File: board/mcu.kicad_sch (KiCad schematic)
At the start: 1 part, among them U101 STM32G0B0CETx

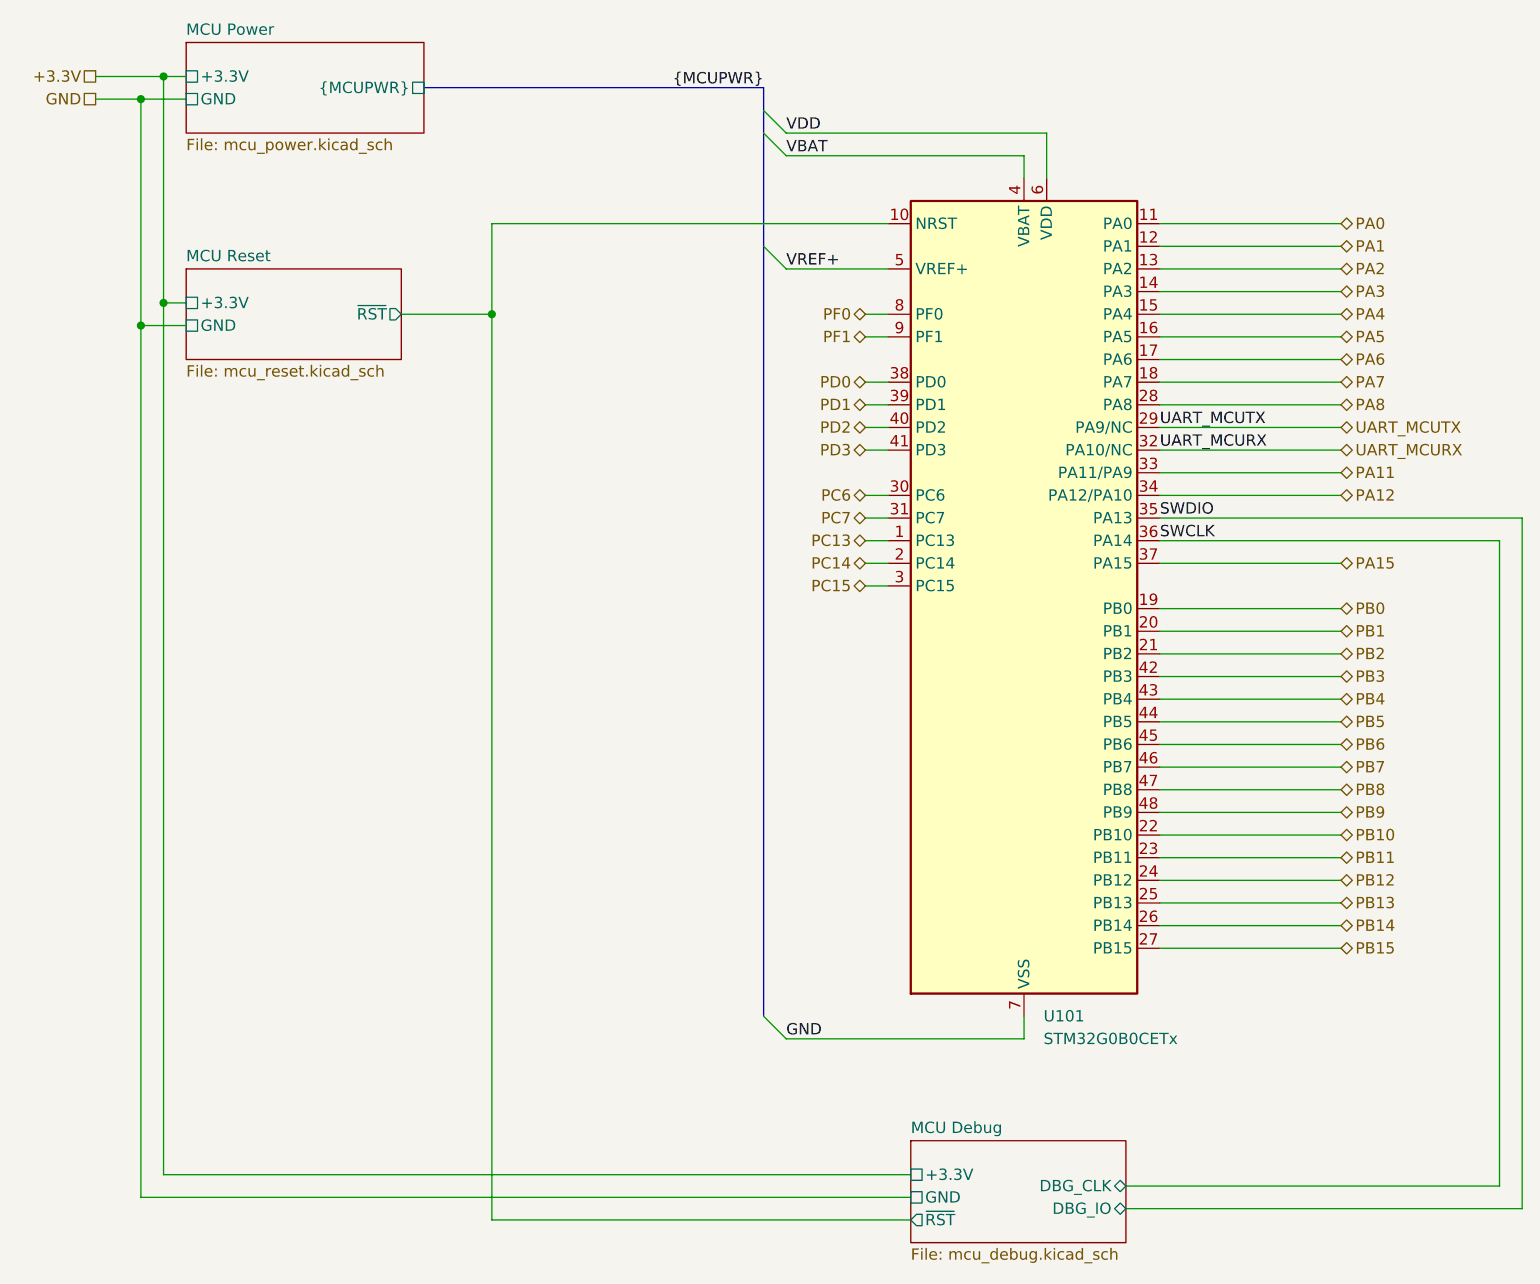
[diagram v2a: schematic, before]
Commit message: redo board to use I2C port expanders (and smaller MCU)
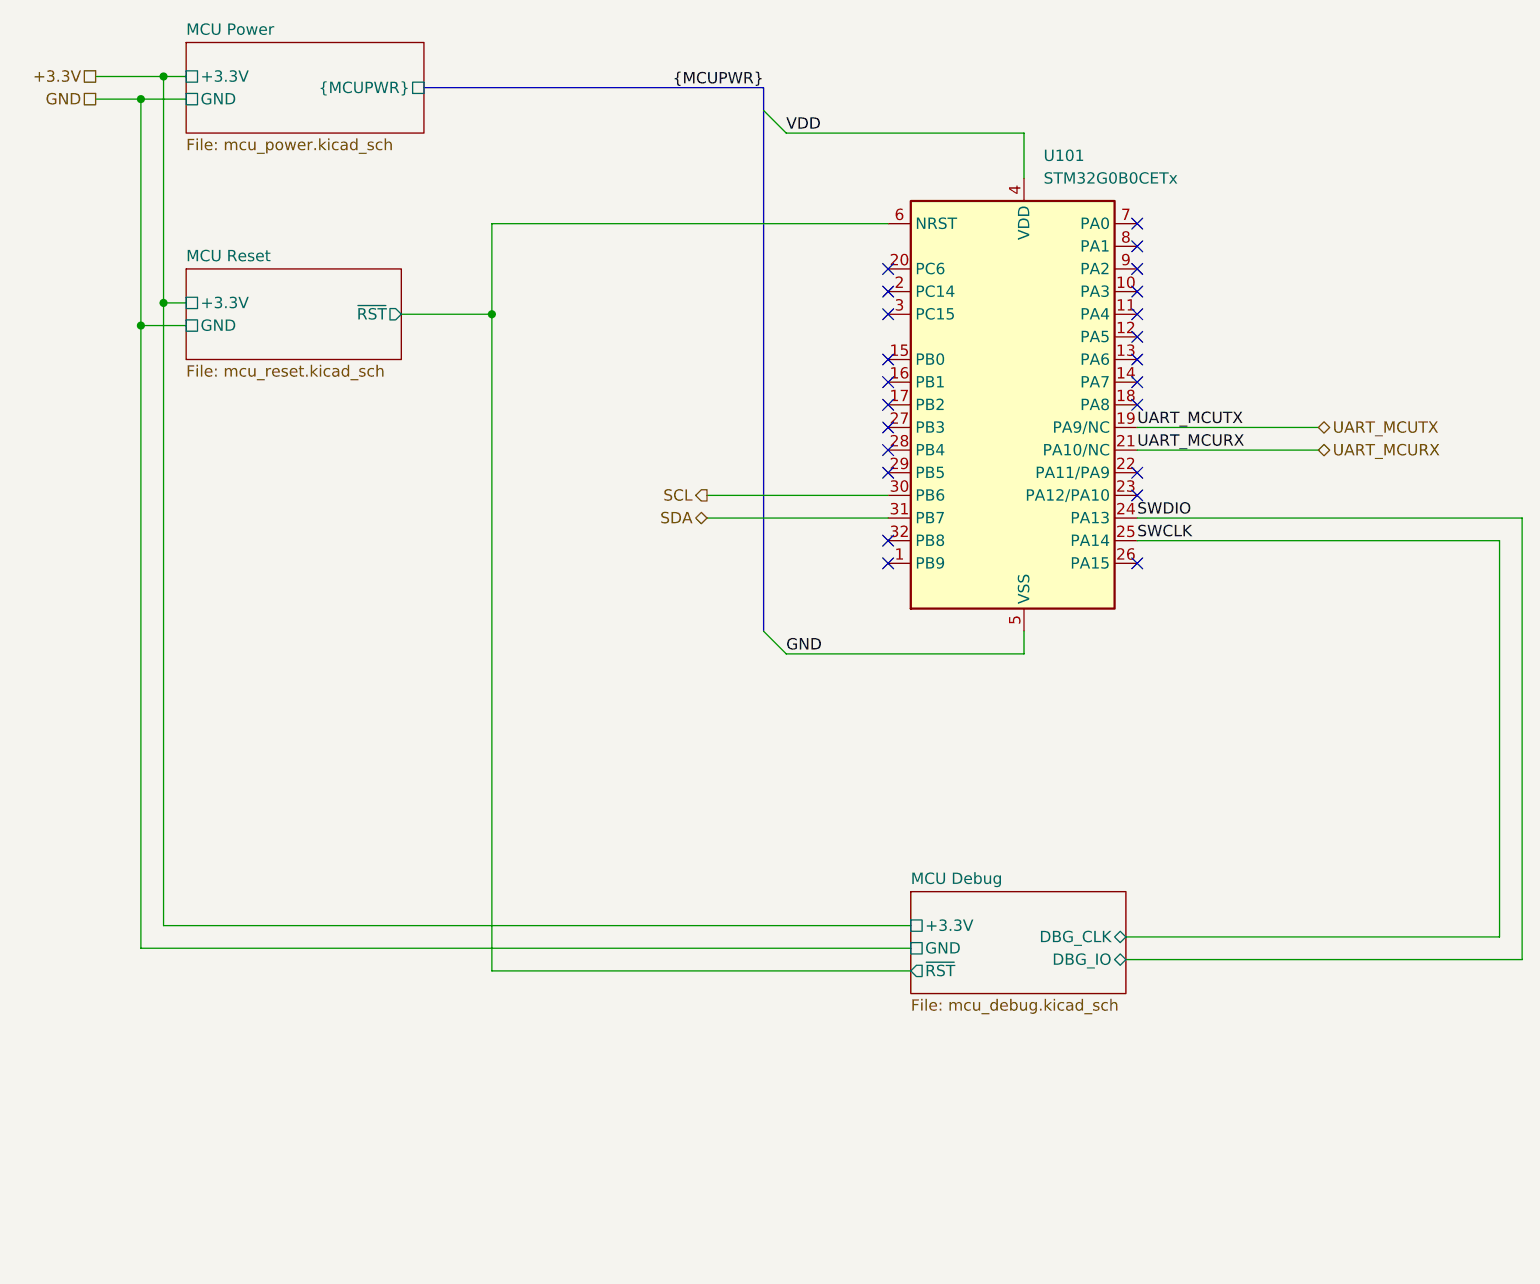
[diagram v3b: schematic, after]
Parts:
- U101: footprint Package_QFP:LQFP-48_7x7mm_P0.5mm -> Package_QFP:LQFP-32_7x7mm_P0.8mm; symbol MCU_ST_STM32G0:STM32G0B0CETx -> MCU_ST_STM32G0:STM32G0B0KETx
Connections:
- net PB0 is gone; now on net UART_MCUTX: U101.19 (PA9/NC)
- net PB12 is gone; now on net SWDIO: U101.24 (PA13)
- net PB13 is gone; now on net SWCLK: U101.25 (PA14)
- net PB2 is gone; now on net UART_MCURX: U101.21 (PA10/NC)
- net VBAT is gone; now on net VDD: U101.4 (VDD)
- net VREF+ is gone; now on net GND: U101.5 (VSS)
- net GND: no longer U101.7 (VSS)
- net MCU Debug/~{RST}: now also U101.6 (NRST); no longer U101.10 (NRST)
- net SWCLK: no longer U101.36 (PA14)
- net SWDIO: no longer U101.35 (PA13)
- net UART_MCURX: no longer U101.32 (PA10/NC)
- net UART_MCUTX: no longer U101.29 (PA9/NC)
- net VDD: no longer U101.6 (VDD)
- net PA0: no longer names the net of U101.11 (PA4)
- net PA1: no longer names the net of U101.12 (PA5)
- removed net PA11: U101.33 (PA11/PA9)
- removed net PA12: U101.34 (PA12/PA10)
- removed net PA15: U101.37 (PA15)
- net PA2: no longer names the net of U101.13 (PA6)
- net PA3: no longer names the net of U101.14 (PA7)
- net PA4: no longer names the net of U101.15 (PB0)
- net PA5: no longer names the net of U101.16 (PB1)
- net PA6: no longer names the net of U101.17 (PB2)
- net PA7: no longer names the net of U101.18 (PA8)
- net PA8: no longer names the net of U101.28 (PB4)
- net PB1: no longer names the net of U101.20 (PC6)
- net PB10: no longer names the net of U101.22 (PA11/PA9)
- net PB11: no longer names the net of U101.23 (PA12/PA10)
- net PB14: no longer names the net of U101.26 (PA15)
- net PB15: no longer names the net of U101.27 (PB3)
- removed net PB3: U101.42 (PB3)
- removed net PB4: U101.43 (PB4)
- removed net PB5: U101.44 (PB5)
- removed net PB6: U101.45 (PB6)
- removed net PB7: U101.46 (PB7)
- removed net PB8: U101.47 (PB8)
- removed net PB9: U101.48 (PB9)
- net PC13: no longer names the net of U101.1 (PB9)
- net PC14: no longer names the net of U101.2 (PC14)
- net PC15: no longer names the net of U101.3 (PC15)
- net PC6 renamed SCL
- net PC7 renamed SDA
- removed net PD0: U101.38 (PD0)
- removed net PD1: U101.39 (PD1)
- removed net PD2: U101.40 (PD2)
- removed net PD3: U101.41 (PD3)
- net PF0: no longer names the net of U101.8 (PA1)
- net PF1: no longer names the net of U101.9 (PA2)
- no-connect marks 0 -> 23

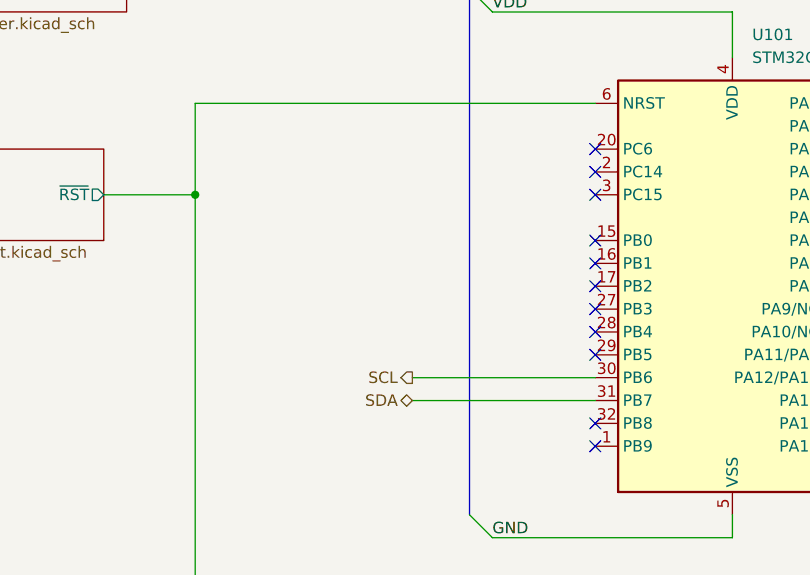
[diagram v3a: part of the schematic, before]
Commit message: allow driving ~RESET pins of I2C I/O expanders, add missing resistors
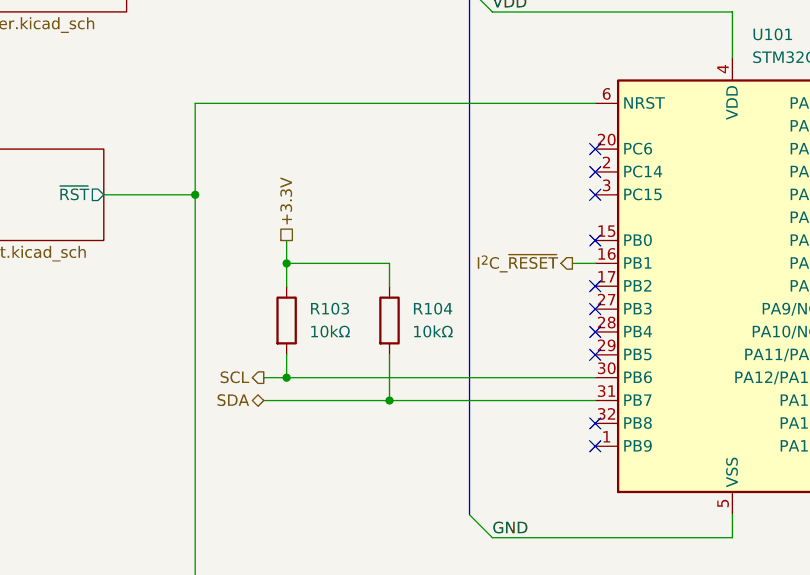
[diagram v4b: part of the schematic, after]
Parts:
- added R103, R104: 10kΩ, Resistor_SMD:R_0402_1005Metric, symbol Device:R
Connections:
- net +3.3V: now also R103.1, R104.1
- net SCL: now also R103.2
- net SDA: now also R104.2
- net I^{2}C_~{RESET}: now reaches U101.16 (PB1)
- no-connect marks 23 -> 22

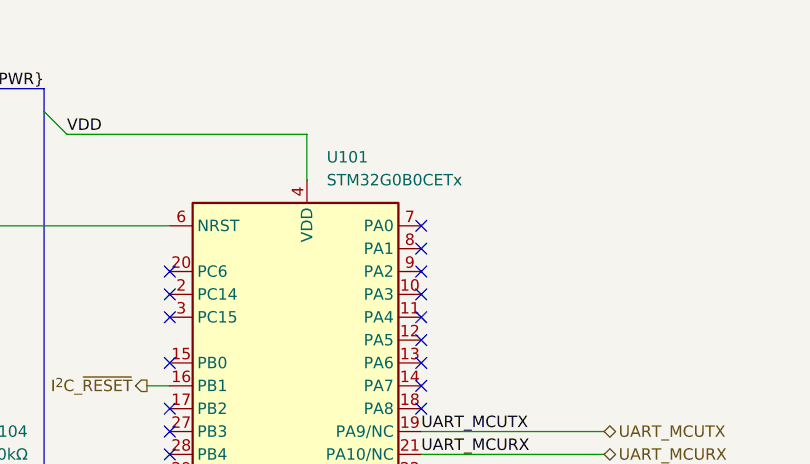
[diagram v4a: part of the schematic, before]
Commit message: update MCU model name
we use the variant with fewer pins now
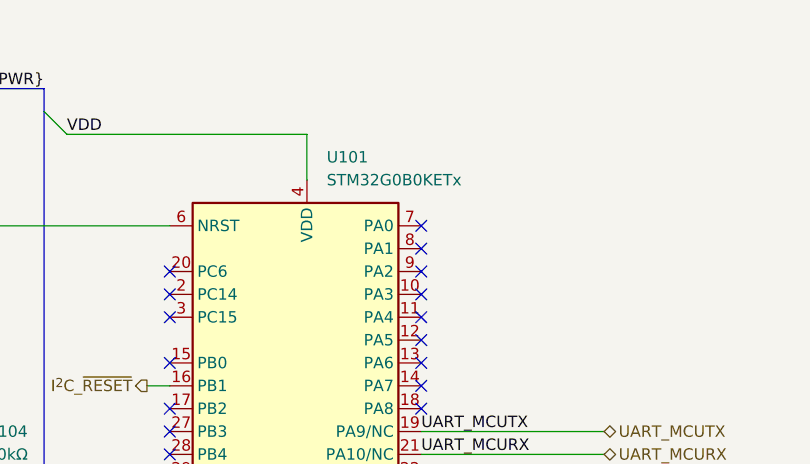
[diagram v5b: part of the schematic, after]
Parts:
- U101: value STM32G0B0CETx -> STM32G0B0KETx
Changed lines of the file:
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@@
 			)
 		)
-		(property "Value" "STM32G0B0CETx"
+		(property "Value" "STM32G0B0KETx"
 			(at 139.3541 49.53 0)
 			(effects

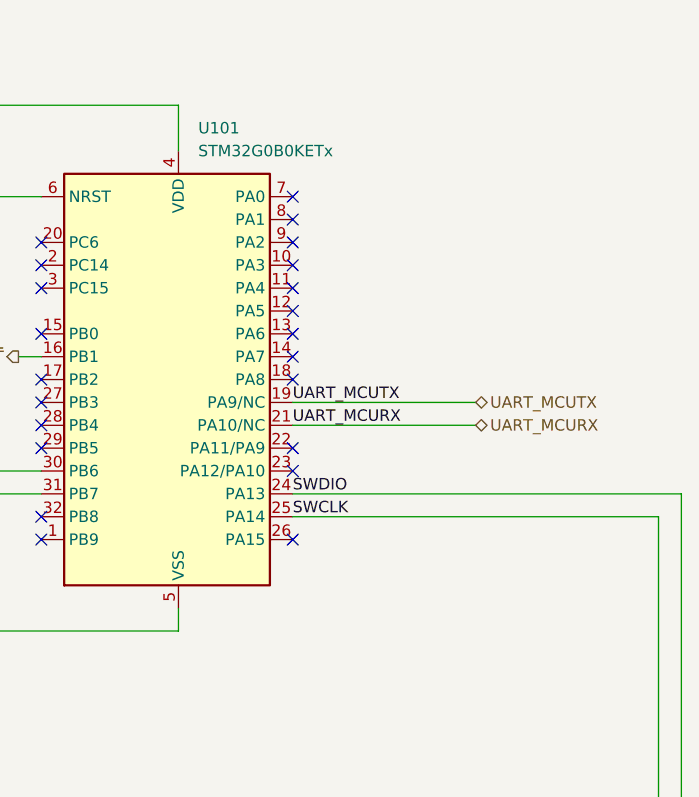
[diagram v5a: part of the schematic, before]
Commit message: add an LED because everything is better with LEDs
also debugging before UART comes up
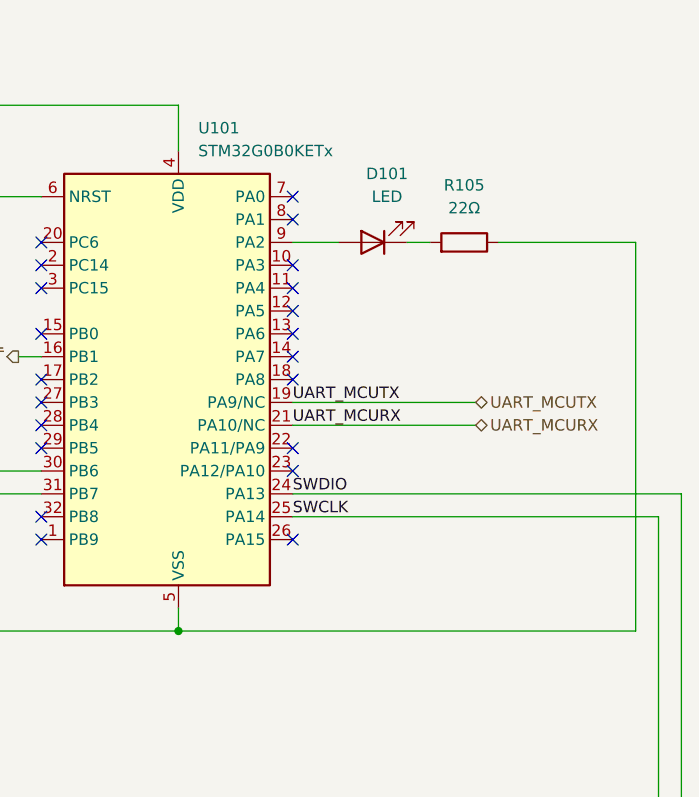
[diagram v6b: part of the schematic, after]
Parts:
- added D101: LED, LED_SMD:LED_0805_2012Metric, symbol Device:LED
- added R105: 22Ω, Resistor_SMD:R_0402_1005Metric, symbol Device:R
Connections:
- net GND: now also R105.1
- net at U101.9 (PA2): now also D101.2 (A)
- new net: D101.1 (K), R105.2
- no-connect marks 22 -> 21
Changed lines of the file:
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@@
+	)
+	(junction
+		(at 137.16 102.87)
+		(diameter 0)
+		(color 0 0 0 0)
 	)
 	(junction
@@
 	)
 	(no_connect
-		(at 149.86 59.69)
-	)
-	(no_connect
 		(at 149.86 92.71)
 	)
@@
 	(wire
 		(pts
+			(xy 137.16 102.87) (xy 187.96 102.87)
+		)
+		(stroke
+			(width 0)
+			(type default)
+		)
+	)
+	(wire
+		(pts
 			(xy 77.47 54.61) (xy 121.92 54.61)
 		)
@@
 	(wire
 		(pts
+			(xy 187.96 102.87) (xy 187.96 59.69)
+		)
+		(stroke
+			(width 0)
+			(type default)
+		)
+	)
+	(wire
+		(pts
 			(xy 193.04 137.16) (xy 193.04 87.63)
 		)
@@
 	(wire
 		(pts
+			(xy 172.72 59.69) (xy 187.96 59.69)
+		)
+		(stroke
+			(width 0)
+			(type default)
+		)
+	)
+	(wire
+		(pts
 			(xy 85.09 85.09) (xy 87.63 85.09)
 		)
@@
 	(wire
 		(pts
+			(xy 162.56 59.69) (xy 165.1 59.69)
+		)
+		(stroke
+			(width 0)
+			(type default)
+		)
+	)
+	(wire
+		(pts
 			(xy 137.16 44.45) (xy 137.16 49.53)
 		)
@@
 		(pts
 			(xy 40.64 38.1) (xy 40.64 63.5)
+		)
+		(stroke
+			(width 0)
+			(type default)
+		)
+	)
+	(wire
+		(pts
+			(xy 149.86 59.69) (xy 154.94 59.69)
 		)
 		(stroke
@@
 			)
 			(justify left)
+		)
+	)
+	(symbol
+		(lib_id "Device:LED")
+		(at 158.75 59.69 180)
+		(unit 1)
+		(exclude_from_sim no)
+		(in_bom yes)
+		(on_board yes)
+		(dnp no)
+		(fields_autoplaced yes)
+		(property "Reference" "D101"
+			(at 160.3375 52.07 0)
+			(effects
+				(font
+					(size 1.27 1.27)
+				)
+			)
+		)
+		(property "Value" "LED"
+			(at 160.3375 54.61 0)
+			(effects
+				(font
+					(size 1.27 1.27)
+				)
+			)
+		)
+		(property "Footprint" "LED_SMD:LED_0805_2012Metric"
+			(at 158.75 59.69 0)
+			(effects
+				(font
+					(size 1.27 1.27)
+				)
+				(hide yes)
+			)
+		)
+		(property "Datasheet" "~"
+			(at 158.75 59.69 0)
+			(effects
+				(font
+					(size 1.27 1.27)
+				)
+				(hide yes)
+			)
+		)
+		(property "Description" "Light emitting diode"
+			(at 158.75 59.69 0)
+			(effects
+				(font
+					(size 1.27 1.27)
+				)
+				(hide yes)
+			)
+		)
+		(pin "1"
+		)
+		(pin "2"
+		)
+		(instances
+			(project "eprom5vread"
+				(path "/b08a8275-42d3-43c1-b04c-f89506e7527b/2fd5d481-fecc-449f-aabd-88adee8fd543"
+					(reference "D101")
+					(unit 1)
+				)
+			)
 		)
 	)
@@
 					(unit 1)
 				)
+			)
+		)
+	)
+	(symbol
+		(lib_id "Device:R")
+		(at 168.91 59.69 270)
+		(mirror x)
+		(unit 1)
+		(exclude_from_sim no)
+		(in_bom yes)
+		(on_board yes)
+		(dnp no)
+		(property "Reference" "R105"
+			(at 168.91 53.34 90)
+			(effects
+				(font
+					(size 1.27 1.27)
+				)
+			)
+		)
+		(property "Value" "22Ω"
+			(at 168.91 55.88 90)
+			(effects
+				(font
+					(size 1.27 1.27)
+				)
+			)
+		)
+		(property "Footprint" "Resistor_SMD:R_0402_1005Metric"
+			(at 168.91 61.468 90)
+			(effects
+				(font
+					(size 1.27 1.27)
+				)
+				(hide yes)
+			)
+		)
+		(property "Datasheet" "~"
+			(at 168.91 59.69 0)
+			(effects
+				(font
+					(size 1.27 1.27)
+				)
+				(hide yes)
+			)
+		)
+		(property "Description" "Resistor"
+			(at 168.91 59.69 0)
+			(effects
+				(font
+					(size 1.27 1.27)
+				)
+				(hide yes)
+			)
+		)
+		(property "LCSC" "C25092"
+			(at 168.91 59.69 0)
+			(effects
+				(font
+					(size 1.27 1.27)
+				)
+				(hide yes)
+			)
+		)
+		(pin "2"
+		)
+		(pin "1"
+		)
+		(instances
+			(project "eprom5vread"
+				(path "/b08a8275-42d3-43c1-b04c-f89506e7527b/2fd5d481-fecc-449f-aabd-88adee8fd543"
+					(reference "R105")
+					(unit 1)
+				)
